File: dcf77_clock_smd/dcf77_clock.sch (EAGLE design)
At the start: 42 parts, among them IC1 7805DT, IC2 ATMEGA48/88/168-AU, J2 DCJ0202, Q1 32.768kHz, Q2 IRLML6244TRPBF, SW1 EC12E_SW, U1 LCD-16X2SILK, U2 DS1307SO8

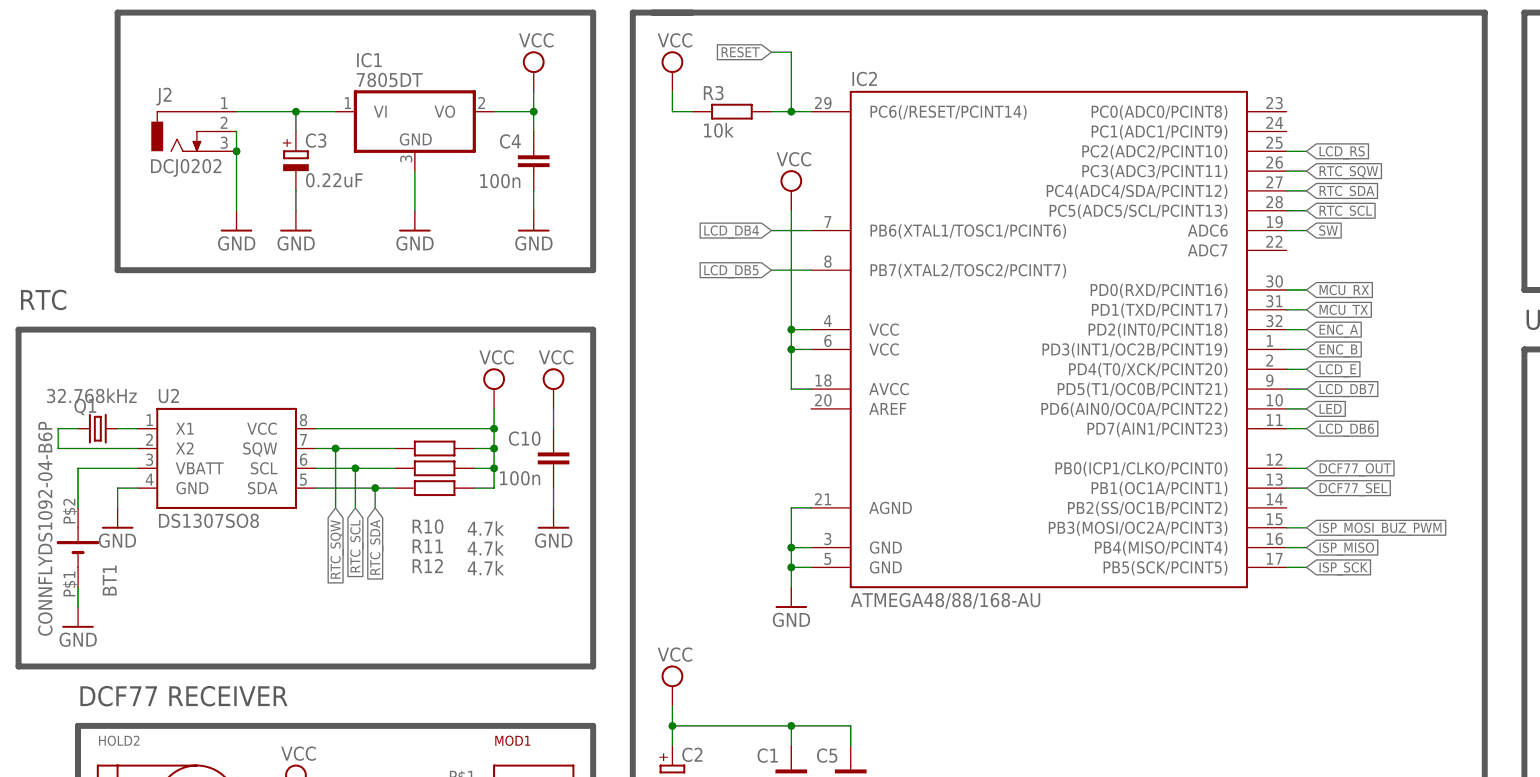
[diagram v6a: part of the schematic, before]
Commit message: Replace incorrect footprints
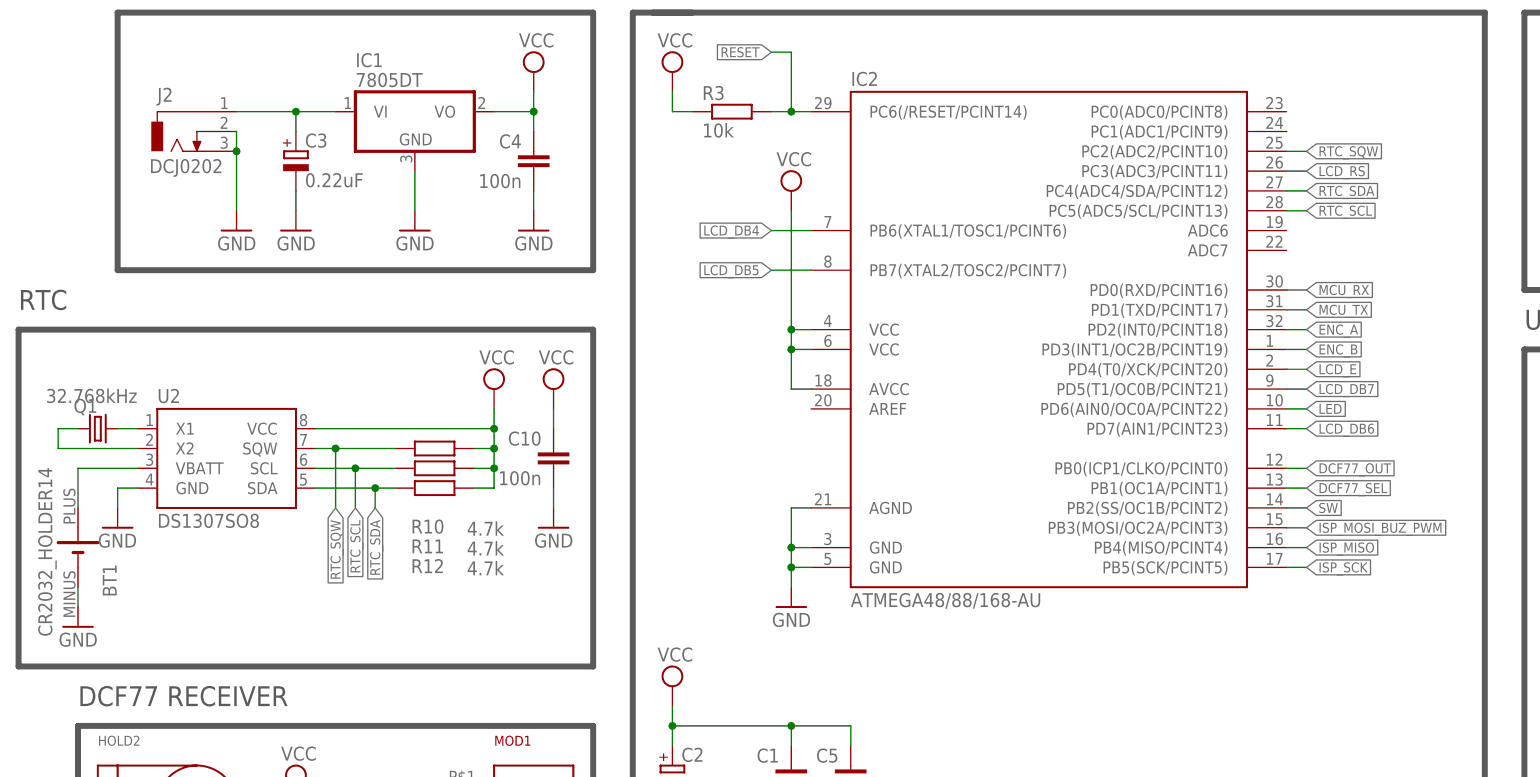
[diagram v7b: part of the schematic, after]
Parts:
- BT1: value CONNFLYDS1092-04-B6P -> CR2032_HOLDER14; device _mlokc:CONNFLYDS1092-04-B6P -> dcf77:CR2032_HOLDER14
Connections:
- net GND: now also BT1.MINUS; no longer BT1.-
- net LCD_RS: now also IC2.PC3(ADC3/PCINT11); no longer IC2.PC2(ADC2/PCINT10)
- net N$12: now also BT1.PLUS; no longer BT1.+
- net RTC_SQW: now also IC2.PC2(ADC2/PCINT10); no longer IC2.PC3(ADC3/PCINT11)
- net SW: now also IC2.PB2(SS/OC1B/PCINT2); no longer IC2.ADC6
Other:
- moved on the sheet: BT1
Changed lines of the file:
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@@
 <part name="H1" library="holes" library_urn="urn:adsk.eagle:library:237" deviceset="MOUNT-HOLE" device="3.2" package3d_urn="urn:adsk.eagle:package:14275/1" value="MOUNT-HOLE3.2"/>
 <part name="D1" library="diode" library_urn="urn:adsk.eagle:library:210" deviceset="DIODE-" device="SOD123" package3d_urn="urn:adsk.eagle:package:43420/1" value="1N4007"/>
-<part name="BT1" library="_mlokc" deviceset="CONNFLYDS1092-04-B6P" device=""/>
+<part name="BT1" library="dcf77" deviceset="CR2032_HOLDER" device="14"/>
 <part name="R3" library="rcl" library_urn="urn:adsk.eagle:library:334" deviceset="R-EU_" device="M0805" package3d_urn="urn:adsk.eagle:package:23556/2" value="10k"/>
 <part name="SUPPLY2" library="supply2" library_urn="urn:adsk.eagle:library:372" deviceset="VCC" device=""/>
@@
 <segment>
 <pinref part="GND18" gate="1" pin="GND"/>
-<pinref part="BT1" gate="G$1" pin="-"/>
+<pinref part="BT1" gate="G$1" pin="MINUS"/>
 <wire x1="-134.62" y1="27.94" x2="-134.62" y2="30.48" width="0.1524" layer="91"/>
 </segment>
@@
 </segment>
 <segment>
-<pinref part="IC2" gate="1" pin="ADC6"/>
-<wire x1="20.32" y1="76.2" x2="22.86" y2="76.2" width="0.1524" layer="91"/>
-<label x="22.86" y="76.2" size="1.27" layer="95" xref="yes"/>
+<pinref part="IC2" gate="1" pin="PB2(SS/OC1B/PCINT2)"/>
+<wire x1="20.32" y1="40.64" x2="22.86" y2="40.64" width="0.1524" layer="91"/>
+<label x="22.86" y="40.64" size="1.27" layer="95" xref="yes"/>
 </segment>
 </net>
@@
 </segment>
 <segment>
-<pinref part="IC2" gate="1" pin="PC2(ADC2/PCINT10)"/>
-<wire x1="20.32" y1="86.36" x2="22.86" y2="86.36" width="0.1524" layer="91"/>
-<label x="22.86" y="86.36" size="1.27" layer="95" xref="yes"/>
+<pinref part="IC2" gate="1" pin="PC3(ADC3/PCINT11)"/>
+<wire x1="20.32" y1="83.82" x2="22.86" y2="83.82" width="0.1524" layer="91"/>
+<label x="22.86" y="83.82" size="1.27" layer="95" xref="yes"/>
 </segment>
 </net>
@@
 <pinref part="U2" gate="G$1" pin="VBATT"/>
 <wire x1="-127" y1="45.72" x2="-134.62" y2="45.72" width="0.1524" layer="91"/>
-<pinref part="BT1" gate="G$1" pin="+"/>
+<pinref part="BT1" gate="G$1" pin="PLUS"/>
 <wire x1="-134.62" y1="45.72" x2="-134.62" y2="40.64" width="0.1524" layer="91"/>
 </segment>
@@
 </segment>
 <segment>
-<pinref part="IC2" gate="1" pin="PC3(ADC3/PCINT11)"/>
-<wire x1="20.32" y1="83.82" x2="22.86" y2="83.82" width="0.1524" layer="91"/>
-<label x="22.86" y="83.82" size="1.27" layer="95" xref="yes"/>
-</segment>
-</net>
+<pinref part="IC2" gate="1" pin="PC2(ADC2/PCINT10)"/>
+<wire x1="20.32" y1="86.36" x2="22.86" y2="86.36" width="0.1524" layer="91"/>
+<label x="22.86" y="86.36" size="1.27" layer="95" xref="yes"/>
+</segment>
+</net>

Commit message: Change oscillator footprint
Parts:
- Q1: device crystal:CRYSTALMM39SL -> crystal:CRYSTALMM20SS
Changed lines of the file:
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@@
 <part name="IC1" library="linear" library_urn="urn:adsk.eagle:library:262" deviceset="78*" device="DT" package3d_urn="urn:adsk.eagle:package:16415/2" technology="05" value="7805DT"/>
 <part name="J2" library="con-jack" library_urn="urn:adsk.eagle:library:154" deviceset="DCJ0202" device="" package3d_urn="urn:adsk.eagle:package:7491/1"/>
-<part name="Q1" library="crystal" library_urn="urn:adsk.eagle:library:204" deviceset="CRYSTAL" device="MM39SL" package3d_urn="urn:adsk.eagle:package:12090/1" value="32.768kHz"/>
+<part name="Q1" library="crystal" library_urn="urn:adsk.eagle:library:204" deviceset="CRYSTAL" device="MM20SS" package3d_urn="urn:adsk.eagle:package:12092/1" value="32.768kHz"/>
 <part name="R1" library="SparkFun" deviceset="TRIMPOT" device="PTH" value="10k"/>
 <part name="H1" library="holes" library_urn="urn:adsk.eagle:library:237" deviceset="MOUNT-HOLE" device="3.2" package3d_urn="urn:adsk.eagle:package:14275/1" value="MOUNT-HOLE3.2"/>
